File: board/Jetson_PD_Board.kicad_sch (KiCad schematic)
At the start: 28 parts, among them J1 USB4081-03-A, J2 768250002, Q1 NTTFS5C673NLTAG, Q2 NTTFS5C673NLTAG, Q3 NTTFS5C673NLTAG, U1 APK43070DKZ-13-FA01, U2 USBLC6-2SC6

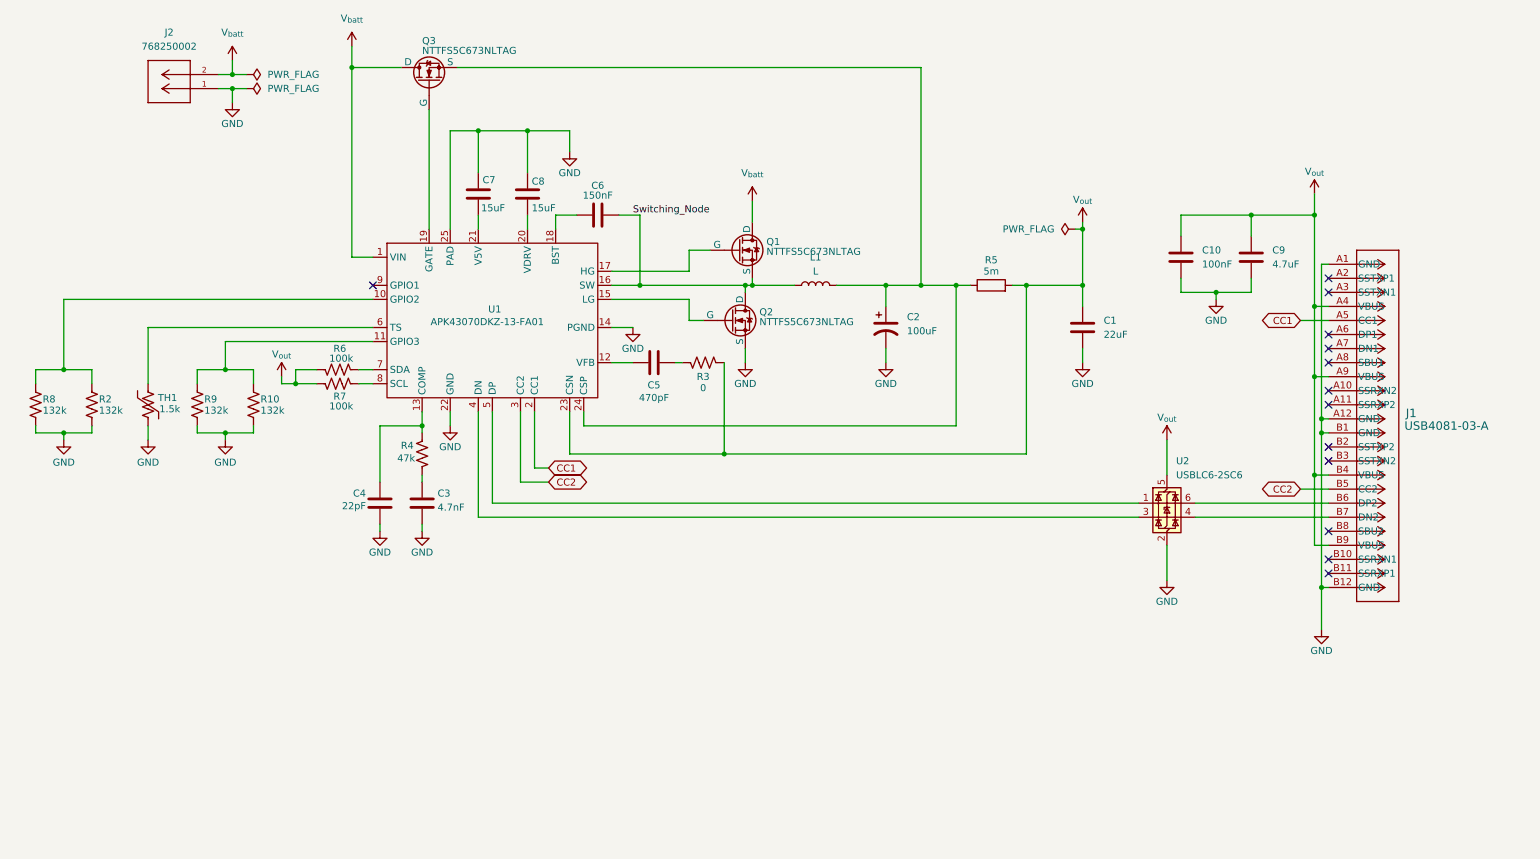
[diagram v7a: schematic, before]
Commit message: Added mounting holes, indicator LED, and cleaned up shcematic
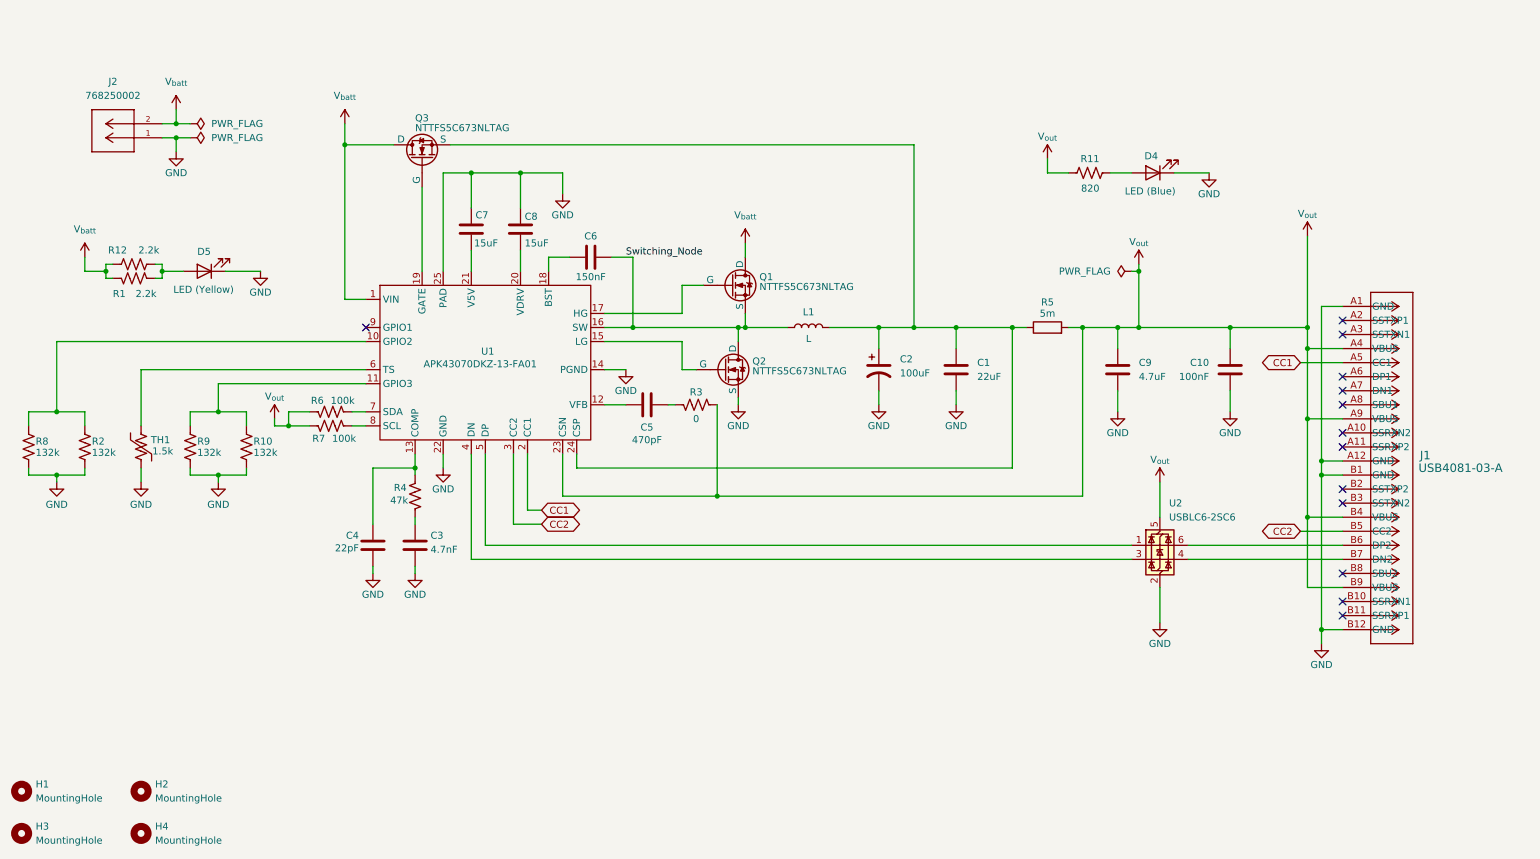
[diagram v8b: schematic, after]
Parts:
- added D4: LED (Blue), LED_SMD:LED_0603_1608Metric, symbol Device:LED
- added D5: LED (Yellow), LED_SMD:LED_0603_1608Metric, symbol Device:LED
- added H1, H2, H3, H4: MountingHole, MountingHole:MountingHole_3.2mm_M3_ISO14580_Pad_TopBottom, symbol Mechanical:MountingHole
- added R1, R12: 2.2k, Resistor_SMD:R_0603_1608Metric_Pad0.98x0.95mm_HandSolder, symbol Device:R_US
- added R11: 820, Resistor_SMD:R_0603_1608Metric_Pad0.98x0.95mm_HandSolder, symbol Device:R_US
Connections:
- net GND: now also D4.1 (K), D5.1 (K)
- net V_{batt}: now also R1.1, R12.1
- net V_{out}: now also R11.1; no longer C1.1
- net at C2.1, L1.2, Q3.3 (S)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: now also C1.1
- new net: D5.2 (A), R1.2, R12.2
- new net: D4.2 (A), R11.2
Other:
- moved on the sheet: C1, C10, C2, C3, C4, C5, C6, C7, C8, C9, J1, J2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
